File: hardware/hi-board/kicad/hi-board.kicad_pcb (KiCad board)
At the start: 4 copper layers, 81 x 117 mm, 69 parts, among them J2 Speaker, SW1 Up, SW2 A, SW3 Down, SW4 B, SW5 Left, SW6 Start, SW7 Right, SW8 Select, U1 LM386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

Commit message: Add GND layer
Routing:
- added copper zone on In2.Cu, net GND

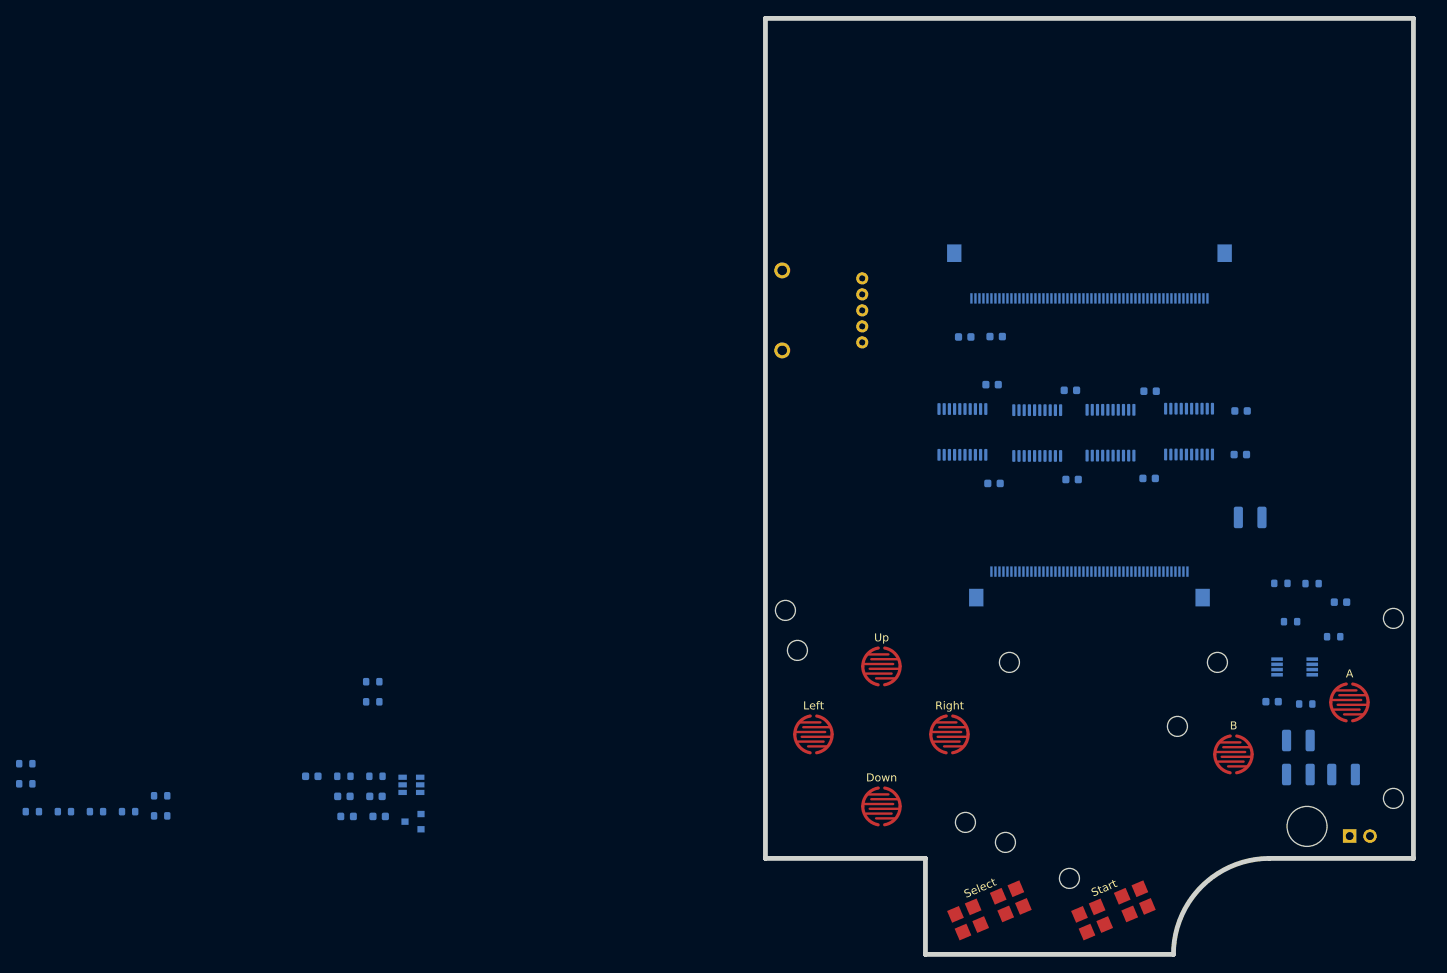
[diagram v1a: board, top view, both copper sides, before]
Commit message: Route all but power rails
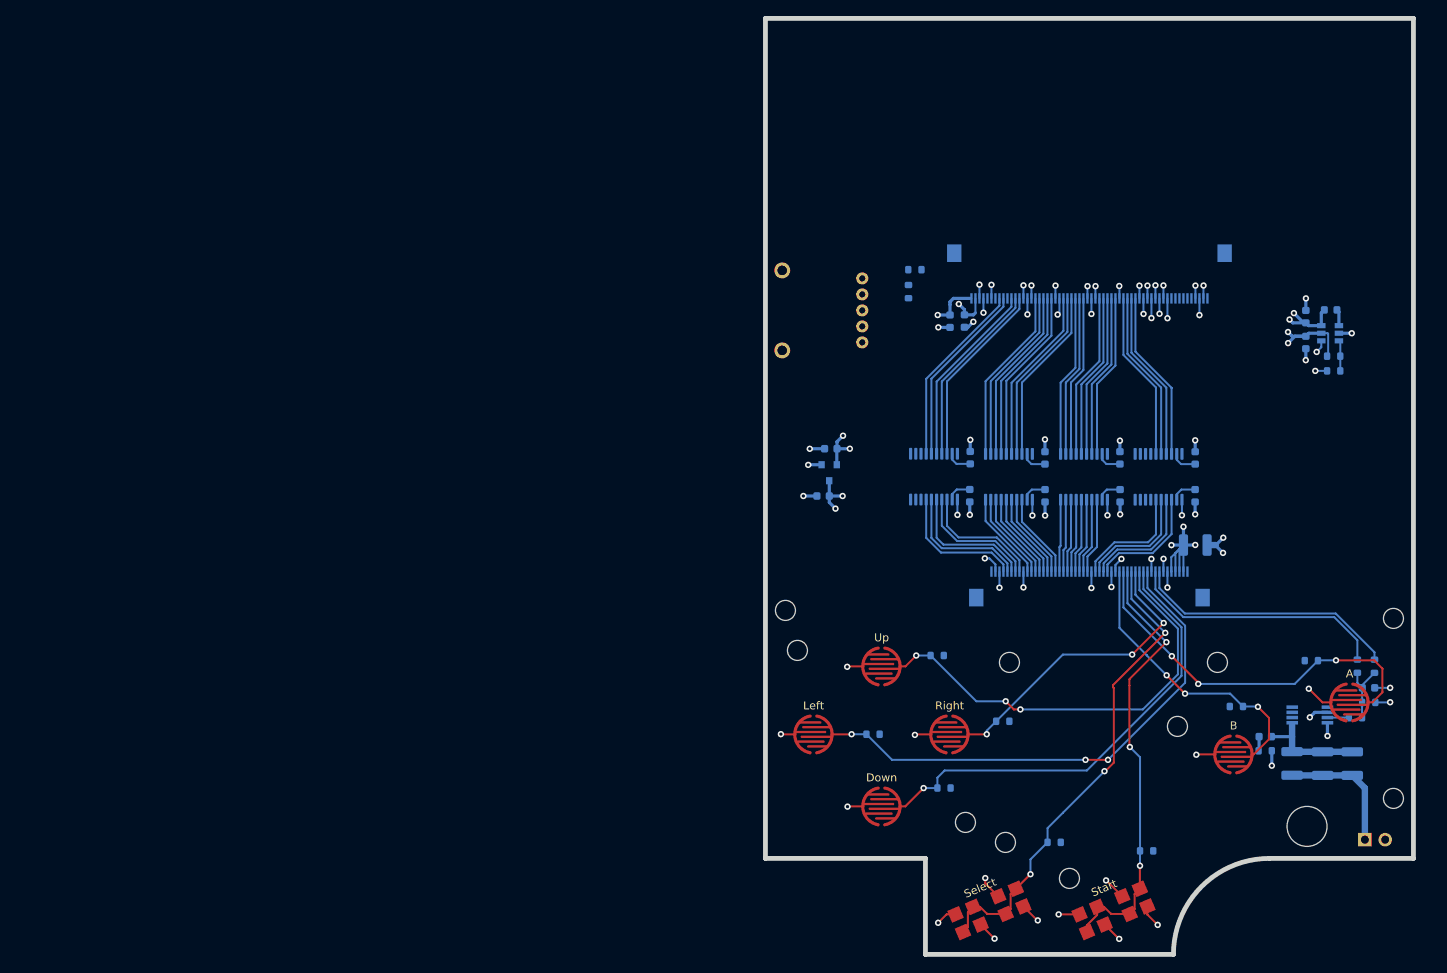
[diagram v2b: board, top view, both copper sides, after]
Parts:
- moved R10 153.0 mm to (68.2, -36.7), turned to 0 degrees
- moved R14 139.4 mm to (47.6, -12.9)
- moved R12 139.1 mm to (58.9, -31.0), turned to 0 degrees
- moved L1 138.3 mm to (70.7, -80.6), turned to 0 degrees
- moved R7 134.4 mm to (71.0, -74.8), turned to 0 degrees
- moved C5 133.0 mm to (67.5, -76.5), turned to 270 degrees
- moved C4 130.8 mm to (67.5, -79.7), turned to 90 degrees
- moved R8 130.0 mm to (71.0, -72.9)
- moved U3 128.0 mm to (70.6, -77.6)
- moved R16 123.8 mm to (36.1, -14.0)
- moved R15 122.2 mm to (29.7, -29.1)
- moved R9 115.0 mm to (21.5, -37.4)
- moved R11 97.9 mm to (22.3, -20.8)
- moved R13 89.6 mm to (13.4, -27.5)
- moved R6 85.1 mm to (18.7, -85.6)
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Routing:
- net GND: track 0.00 -> 142.4 mm, vias 0 -> 74
- net JOY_LEFT: track 0.00 -> 65.3 mm, vias 0 -> 3
- net JOY_SELECT: track 0.00 -> 61.1 mm, vias 0 -> 3
- net JOY_DOWN: track 0.00 -> 57.7 mm, vias 0 -> 1
- net JOY_START: track 0.00 -> 55.9 mm, vias 0 -> 3
- net JOY_UP: track 0.00 -> 54.7 mm, vias 0 -> 3
- net JOY_A: track 0.00 -> 47.9 mm, vias 0 -> 3
- net JOY_RIGHT: track 0.00 -> 38.4 mm, vias 0 -> 3
- net JOY_B: track 0.00 -> 36.0 mm, vias 0 -> 3
- net VOUT: track 0.00 -> 35.4 mm, vias 0 -> 8
- net AUD_R: track 0.00 -> 33.2 mm
- net AUD_L: track 0.00 -> 32.5 mm
- net +3V0: track 0.00 -> 29.4 mm, vias 0 -> 4
- net Net-(U2-Pad11): track 0.00 -> 23.3 mm
- net Net-(U2-Pad12): track 0.00 -> 23.2 mm
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- added copper zone on In1.Cu, net VOUT

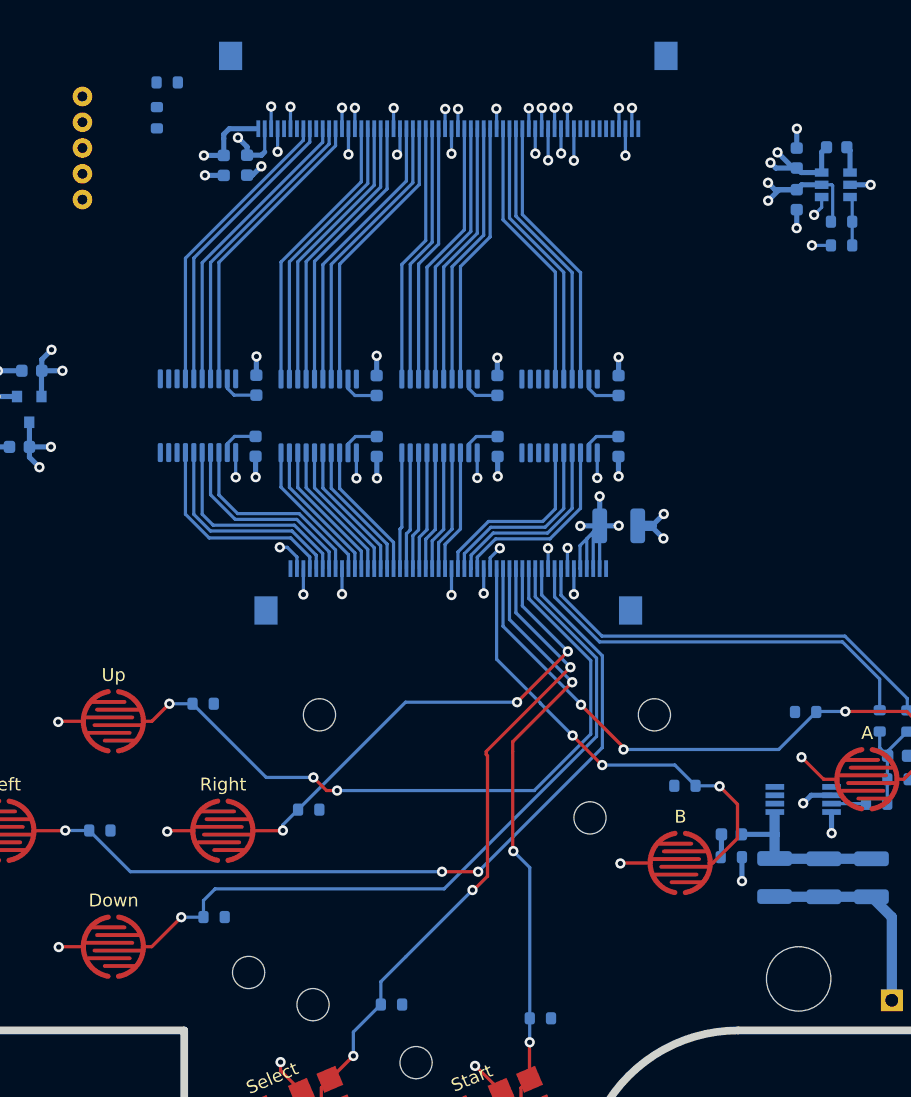
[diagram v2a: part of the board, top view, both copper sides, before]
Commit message: Complete routing of HI board
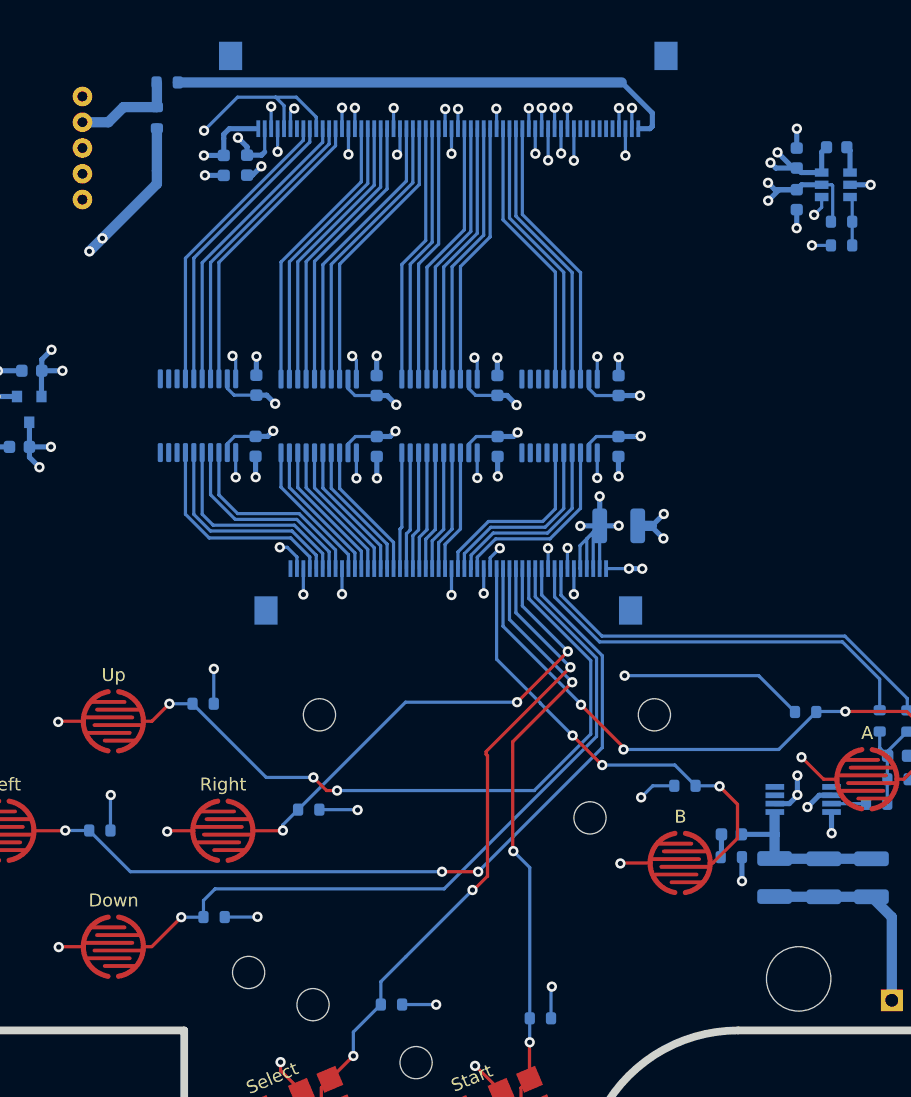
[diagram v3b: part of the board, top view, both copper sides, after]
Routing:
- net +3V3: track 12.7 -> 212.0 mm, vias 0 -> 18
- net Net-(R6-Pad1): track 0.00 -> 40.0 mm
- net +3V0: track 29.4 -> 50.4 mm, vias 4 -> 9
- net +12V: track 10.9 -> 26.1 mm, vias 2 -> 6
- net Net-(R17-Pad2): track 0.00 -> 8.19 mm
- added copper zone on In1.Cu, net +12V
- added copper zone on In1.Cu, net +3V0
- added copper zone on In1.Cu, net +3V3

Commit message: Add logo and rev
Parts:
- added G***: LOGO, hi-board:FPGAMB0, B.Cu at (40.5, -104.0)
- added G***: LOGO, hi-board:FPGAMB0_S, F.Cu at (40.5, -21.0)
- BOARD CONN: renamed from BOARD1
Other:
- board text added: "BOARD B - REV 1"

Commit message: Add testpoints
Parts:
- added TP1: GND, TestPoint:TestPoint_THTPad_1.5x1.5mm_Drill0.7mm, B.Cu at (17.4, -93.9)
- added TP2: GND, TestPoint:TestPoint_THTPad_1.5x1.5mm_Drill0.7mm, B.Cu at (6.46, -49.4)
- added TP3: GND, TestPoint:TestPoint_THTPad_1.5x1.5mm_Drill0.7mm, B.Cu at (54.7, -71.5)
- added TP4: VOUT, TestPoint:TestPoint_THTPad_1.0x1.0mm_Drill0.5mm, B.Cu at (14.6, -44.8)
- added TP5: 3V0, TestPoint:TestPoint_THTPad_1.0x1.0mm_Drill0.5mm, B.Cu at (14.2, -63.2)
- added TP6: 3V3, TestPoint:TestPoint_THTPad_1.0x1.0mm_Drill0.5mm, B.Cu at (14.3, -57.6)
- added TP7: 12V, TestPoint:TestPoint_THTPad_1.0x1.0mm_Drill0.5mm, B.Cu at (72.5, -59.9)

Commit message: Update PCB outline
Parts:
- removed the REF** at (81.0, -27.8)
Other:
- outline, holes or cut-outs redrawn

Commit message: Fix missing connection on hi board
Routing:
- net VOUT: track 35.4 -> 43.7 mm
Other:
- board text added: "BOARD B - REV 2"
- board text removed: "BOARD B - REV 1"
